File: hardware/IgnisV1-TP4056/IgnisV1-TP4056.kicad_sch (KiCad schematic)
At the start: 10 parts, among them SW1 SW-18030, U3 ATtiny212-SS

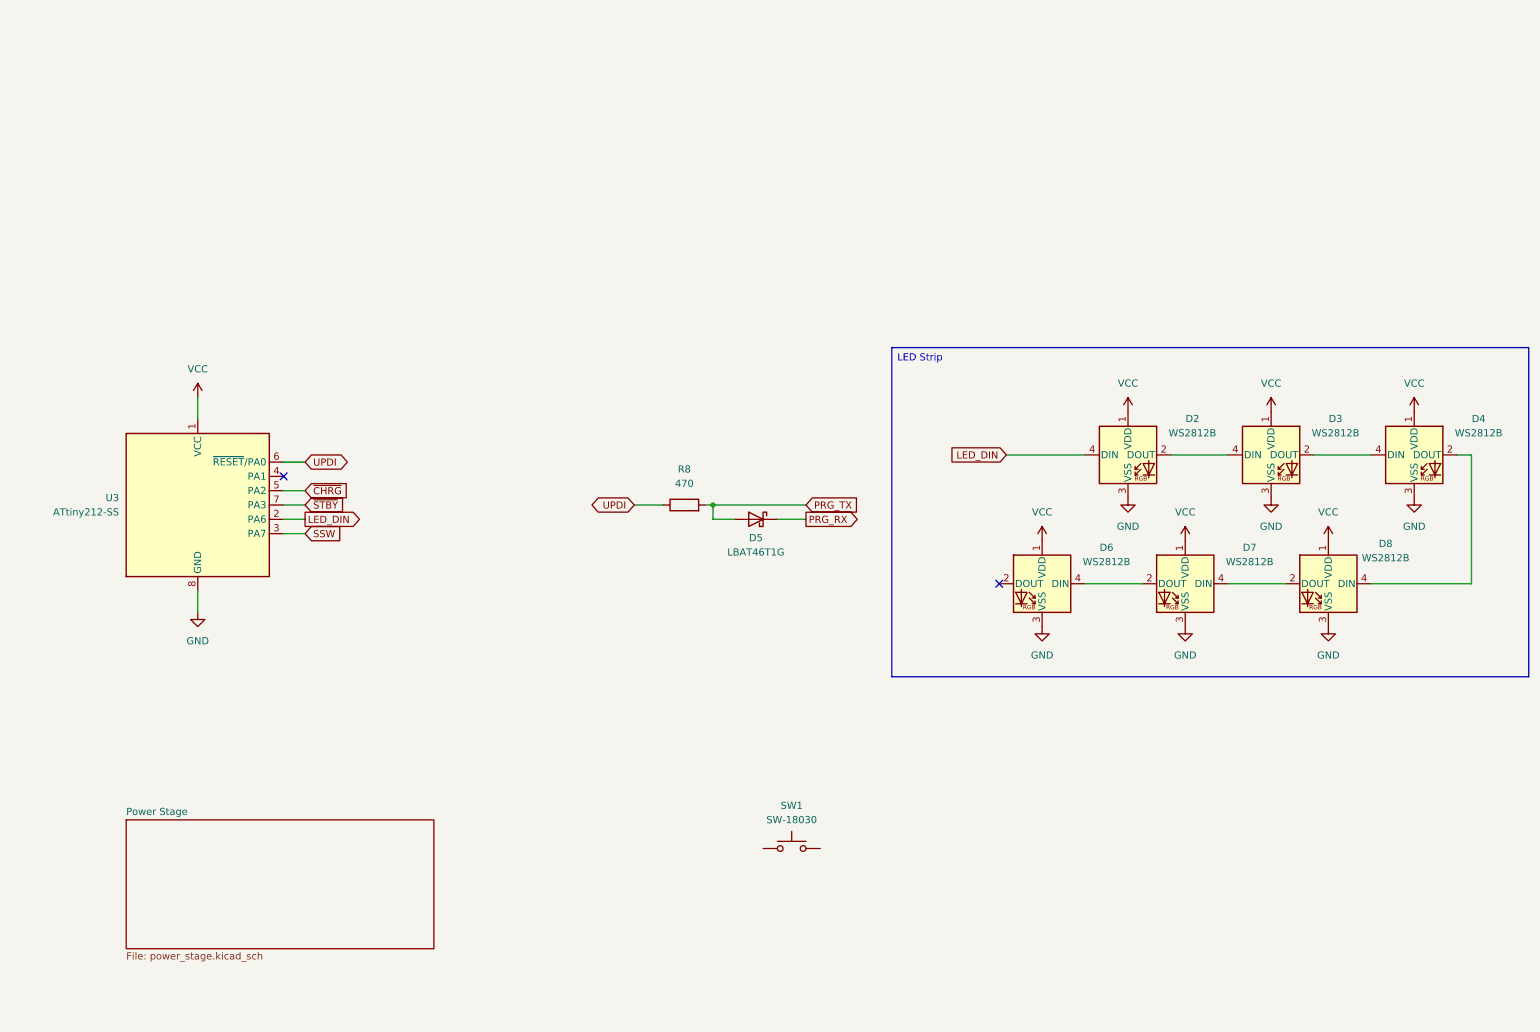
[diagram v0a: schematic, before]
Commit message: ⚡ Rework LED strip and add shock switch filtering
Includes rework of the LED strip
Includes filter with schmidt trigger buffer to input shock switch SW18030
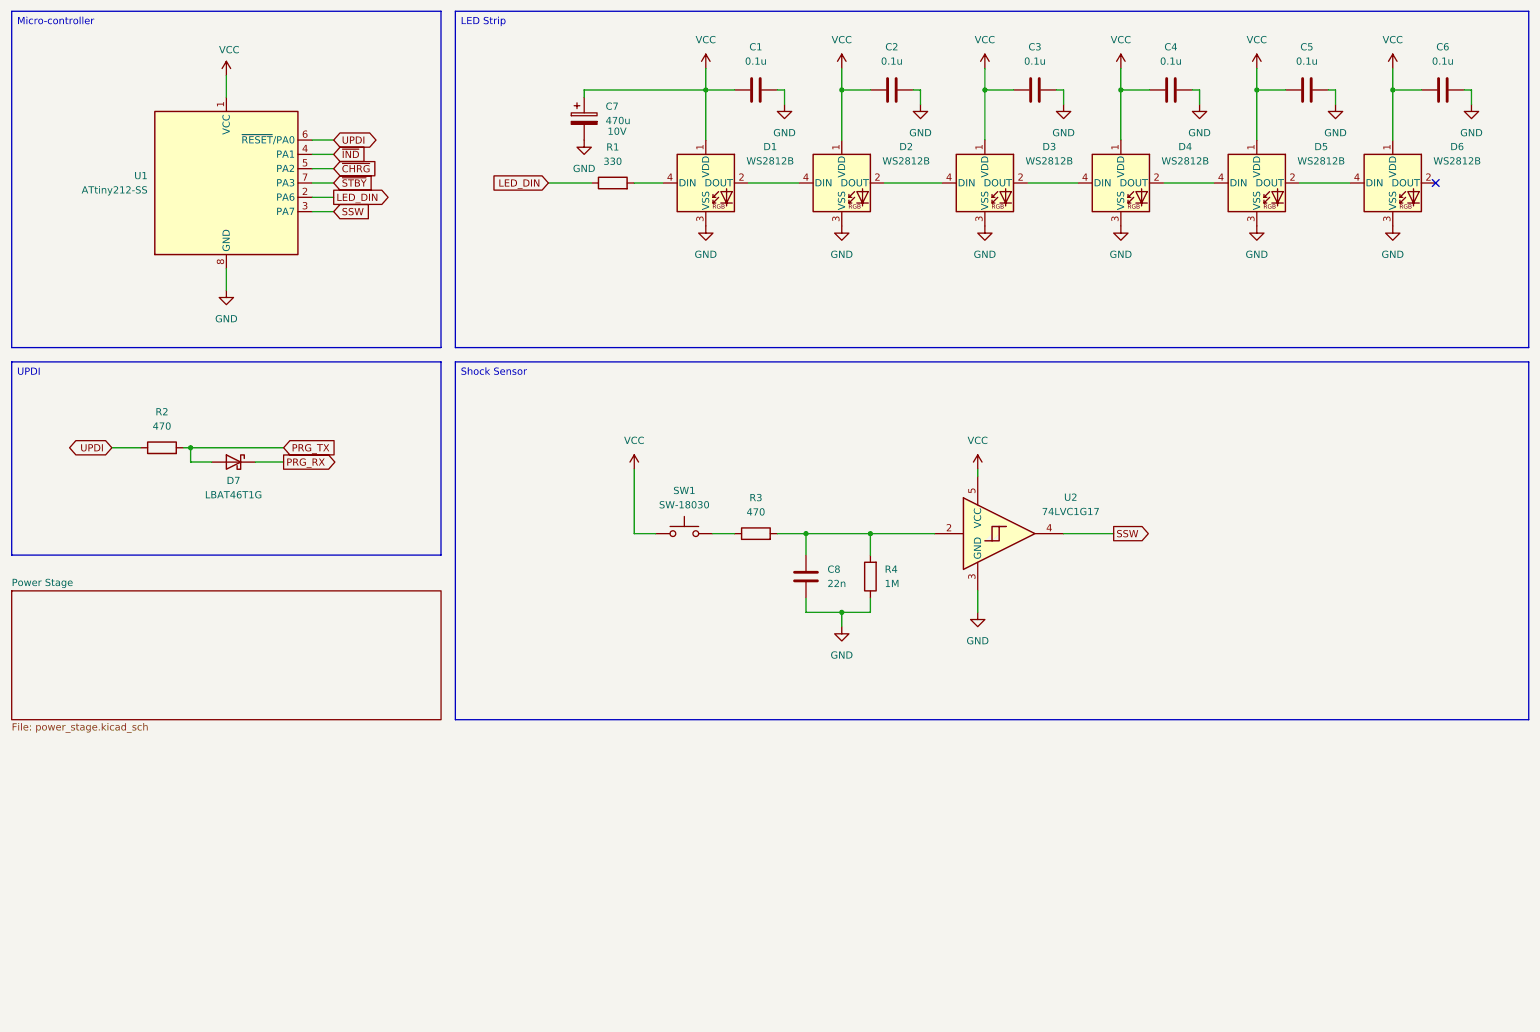
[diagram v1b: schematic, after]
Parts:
- removed D7, D8: WS2812B, LED_SMD:LED_WS2812B_PLCC4_5.0x5.0mm_P3.2mm, symbol LED:WS2812B
- added C1, C2, C3, C4, C5, C6: 0.1u, symbol Device:C
- added C7: 470u, symbol Device:C_Polarized
- added C8: 22n, symbol Device:C
- added D3, D5: WS2812B, LED_SMD:LED_WS2812B_PLCC4_5.0x5.0mm_P3.2mm, symbol LED:WS2812B
- added R1: 330, symbol Device:R
- added R3: 470, symbol Device:R
- added R4: 1M, symbol Device:R
- added U2: 74LVC1G17, symbol 74xGxx:74LVC1G17
- renumbered D2 to D1, D3 to D2, D5 to D7, R8 to R2, U3 to U1
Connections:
- net GND: now also C1.2, C2.2, C3.2, C4.2, C5.2, C6.2, C7.2, C8.2, D3.3 (VSS), D5.3 (VSS), R4.1, U2.3 (GND)
- net LED_DIN: now also R1.1; no longer D1.4 (DIN)
- net SSW: now also U2.4
- net VCC: now also SW1.1, C1.1, C2.1, C3.1, C4.1, C5.1, C6.1, C7.1, D3.1 (VDD), D5.1 (VDD), U2.5 (VCC)
- net at D4.2 (DOUT): now also D5.4 (DIN)
- net at D2.2 (DOUT): now also D3.4 (DIN); no longer D4.4 (DIN)
- net ~{IND}: now reaches U1.4 (PA1)
- net at D6.4 (DIN): now also D5.2 (DOUT)
- net at SW1.2: now also R3.1
- new net: C8.1, R3.2, R4.2, U2.2
- new net: D1.4 (DIN), R1.2
- new net: D3.2 (DOUT), D4.4 (DIN)
- no-connect marks 2 -> 1
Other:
- moved on the sheet: D1, D2, D7, R2, SW1, U1

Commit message: 🧩 Finalize IgnisV1-TP4056 schematics & add reference design
- Finished schematics by adding necessary pull-ups on signal lines.
- Copied electrical design from an older version for reference and traceability.
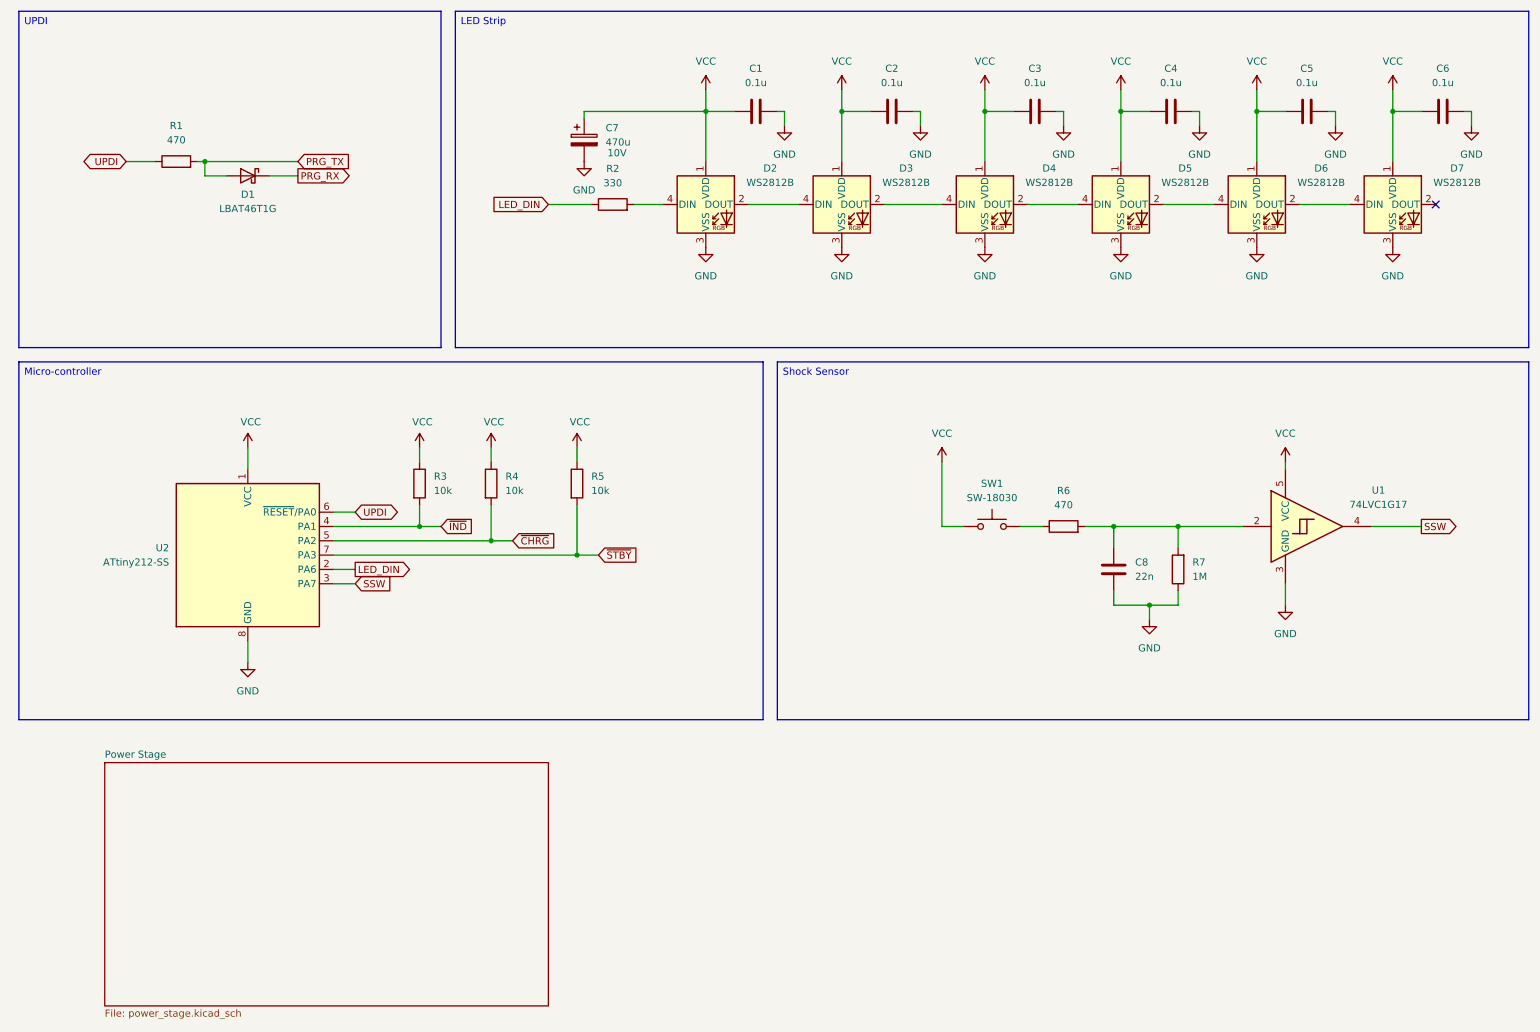
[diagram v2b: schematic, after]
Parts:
- added R3, R4, R5: 10k, symbol Device:R
- renumbered D7 to D1, D1 to D2, D2 to D3, D3 to D4, D4 to D5, D5 to D6, D6 to D7, R2 to R1, R1 to R2, R3 to R6, R4 to R7, U2 to U1, U1 to U2
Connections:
- net VCC: now also R3.1, R4.1, R5.1
- net ~{CHRG}: now also R4.2
- net ~{IND}: now also R3.2
- net ~{STBY}: now also R5.2
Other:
- moved on the sheet: C1, C2, C3, C4, C5, C6, C7, C8, D1, D2, D3, D4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

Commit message: 🎨 Complete logo cleanup and rebranding with new typography
- Changed official logo font from Museo Rounded to "Dongle" Bold
- Reorganized logo assets with consistent naming convention
- Added Makefile for automated PNG export in multiple variants and sizes
- Updated KiCAD worksheets for both IgnisV1 and IgnisV2 PCBs with new branding
- Removed obsolete logo files and consolidated SVG sources
- Exported updated schematic PDFs with refreshed corporate identity
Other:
- title: (none) -> Ignis
